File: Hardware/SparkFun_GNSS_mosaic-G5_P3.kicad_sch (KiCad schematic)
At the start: 65 parts, among them J1 USB_C_Receptacle, J10 U.FL, J2 Conn_01x06, J4 Conn_01x10, J5 SMA_Edge, J6 Conn_01x11, J8 JST_Locking_4, U1 DT1042-04SO, U2 RT9080-3.3, U3 mosaic-G5 P3

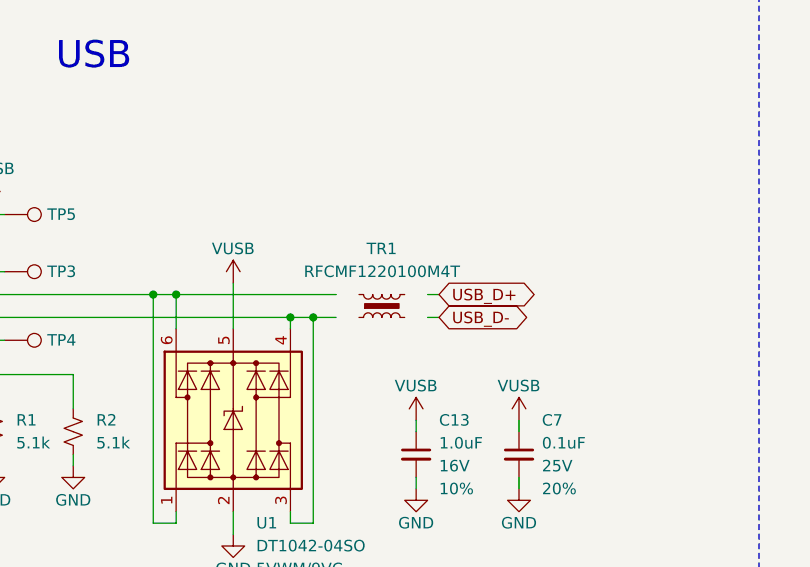
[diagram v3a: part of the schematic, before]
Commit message: Fix RFCMF1220100M4T pin numbering
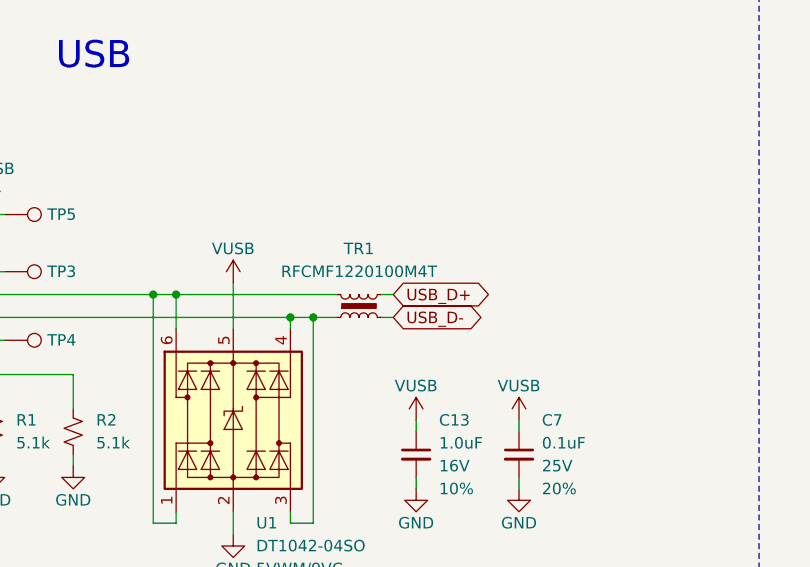
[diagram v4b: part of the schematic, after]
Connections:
- net USB_D+: now also TR1.4
- net USB_D-: now also TR1.2
- net at TR1.1: now also J1.A7 (D-), J1.B7 (D-), TP4.1, U1.3 (I/O2), U1.4 (I/O3)
- net at J1.A6 (D+), J1.B6 (D+), TP3.1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: now also TR1.3
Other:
- moved on the sheet: TR1
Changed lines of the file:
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@@
 	(wire
 		(pts
-			(xy 110.49 52.07) (xy 111.76 52.07)
+			(xy 105.41 52.07) (xy 106.68 52.07)
 		)
 		(stroke
@@
 	(wire
 		(pts
-			(xy 110.49 49.53) (xy 111.76 49.53)
+			(xy 105.41 49.53) (xy 106.68 49.53)
 		)
 		(stroke
@@
 	(global_label "USB_D-"
 		(shape bidirectional)
-		(at 111.76 52.07 0)
+		(at 106.68 52.07 0)
 		(fields_autoplaced yes)
 		(effects
@@
 		)
 		(property "Intersheetrefs" "${INTERSHEET_REFS}"
-			(at 122.6635 52.07 0)
+			(at 117.5835 52.07 0)
 			(effects
 				(font
@@
 	(global_label "USB_D+"
 		(shape bidirectional)
-		(at 111.76 49.53 0)
+		(at 106.68 49.53 0)
 		(fields_autoplaced yes)
 		(effects
@@
 		)
 		(property "Intersheetrefs" "${INTERSHEET_REFS}"
-			(at 122.6635 49.53 0)
+			(at 117.5835 49.53 0)
 			(effects
 				(font
@@
 	(symbol
 		(lib_id "SparkFun-Coil:USB_Transformer")
-		(at 105.41 50.8 0)
+		(at 102.87 50.8 0)
 		(mirror x)
 		(unit 1)
@@
 		(fields_autoplaced yes)
 		(property "Reference" "TR1"
-			(at 105.41 44.45 0)
+			(at 102.87 44.45 0)
 			(effects
 				(font
@@
 		)
 		(property "Value" "RFCMF1220100M4T"
-			(at 105.41 46.99 0)
+			(at 102.87 46.99 0)
 			(effects
 				(font
@@
 		)
 		(property "Footprint" "SparkFun-Coil:Choke_100MHz_USB"
-			(at 104.14 44.45 0)
+			(at 101.6 44.45 0)
 			(effects
 				(font
@@
 		)
 		(property "Datasheet" "http://www.passivecomponent.com/wp-content/uploads/2018/10/RF-Filter.pdf"
-			(at 104.14 41.91 0)
+			(at 101.6 41.91 0)
 			(effects
 				(font
@@
 		)
 		(property "Description" "USB Transformer"
-			(at 105.41 36.83 0)
+			(at 102.87 36.83 0)
 			(effects
 				(font
@@
 		)
 		(property "PROD_ID" "COMP-19495"
-			(at 104.14 39.37 0)
+			(at 101.6 39.37 0)
 			(effects
 				(font
@@
 		(pin "2"
 		)
-		(pin "1"
+		(pin "4"
 		)
-		(pin "2"
+		(pin "3"
 		)
 		(instances

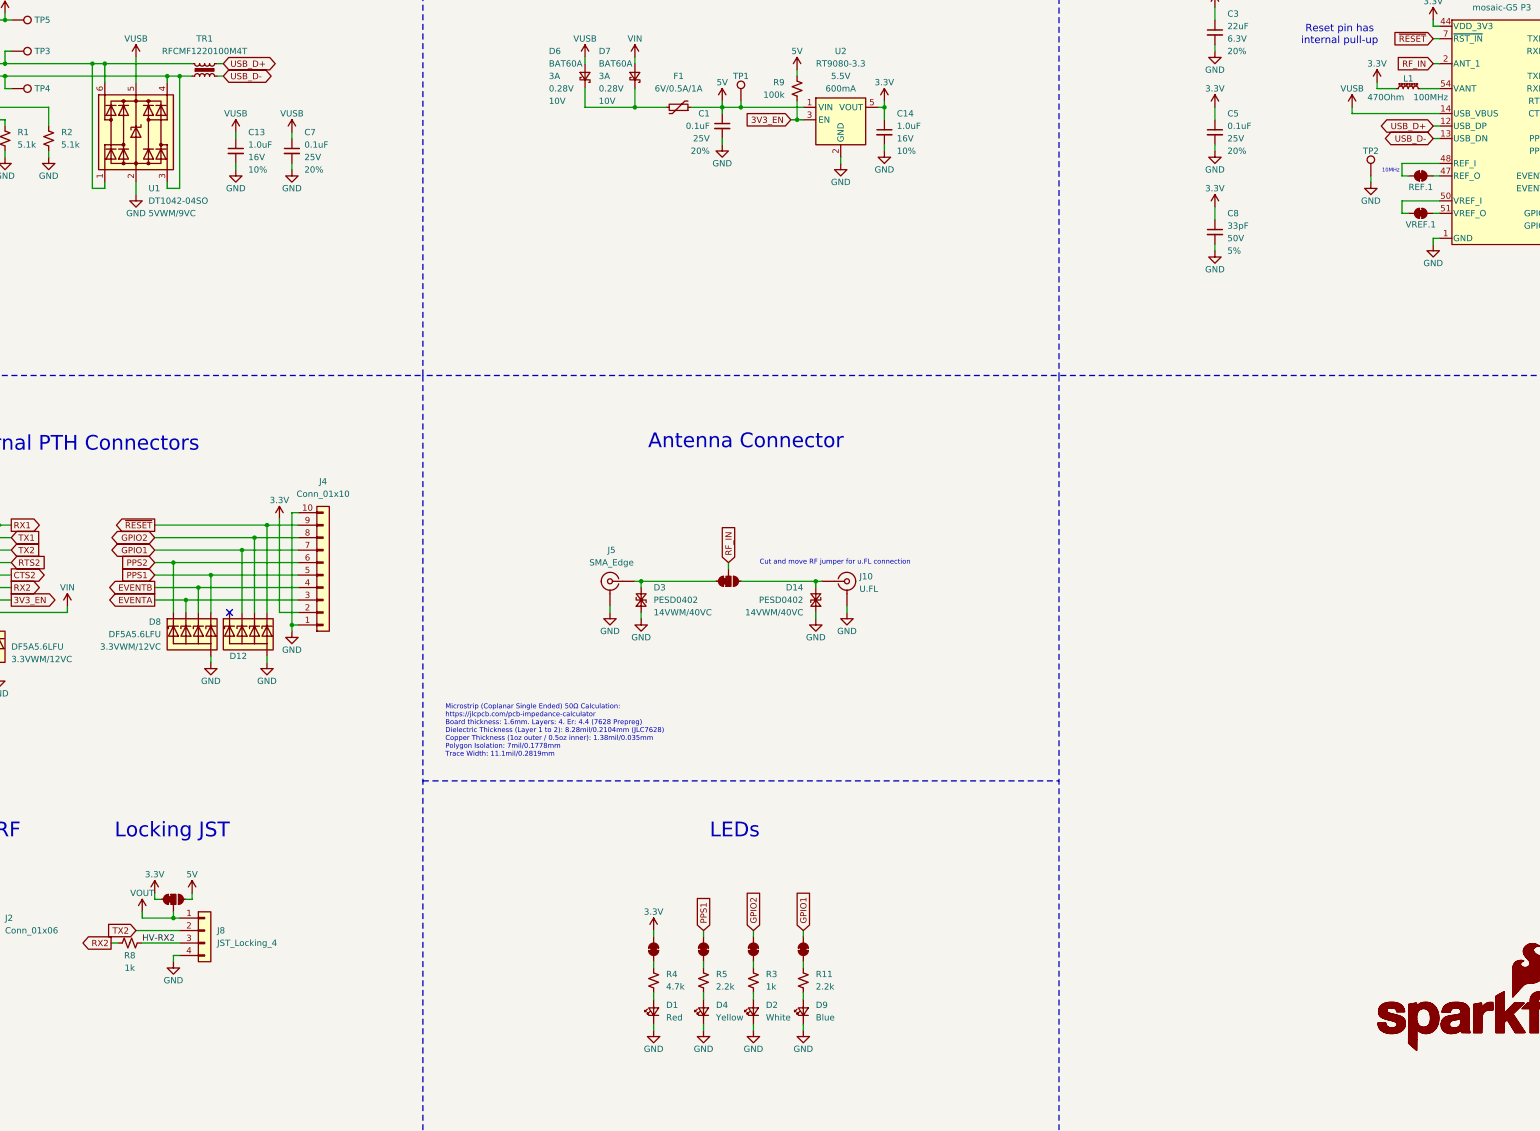
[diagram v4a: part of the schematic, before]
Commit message: Update to latest SparkFun KiCad Libraries
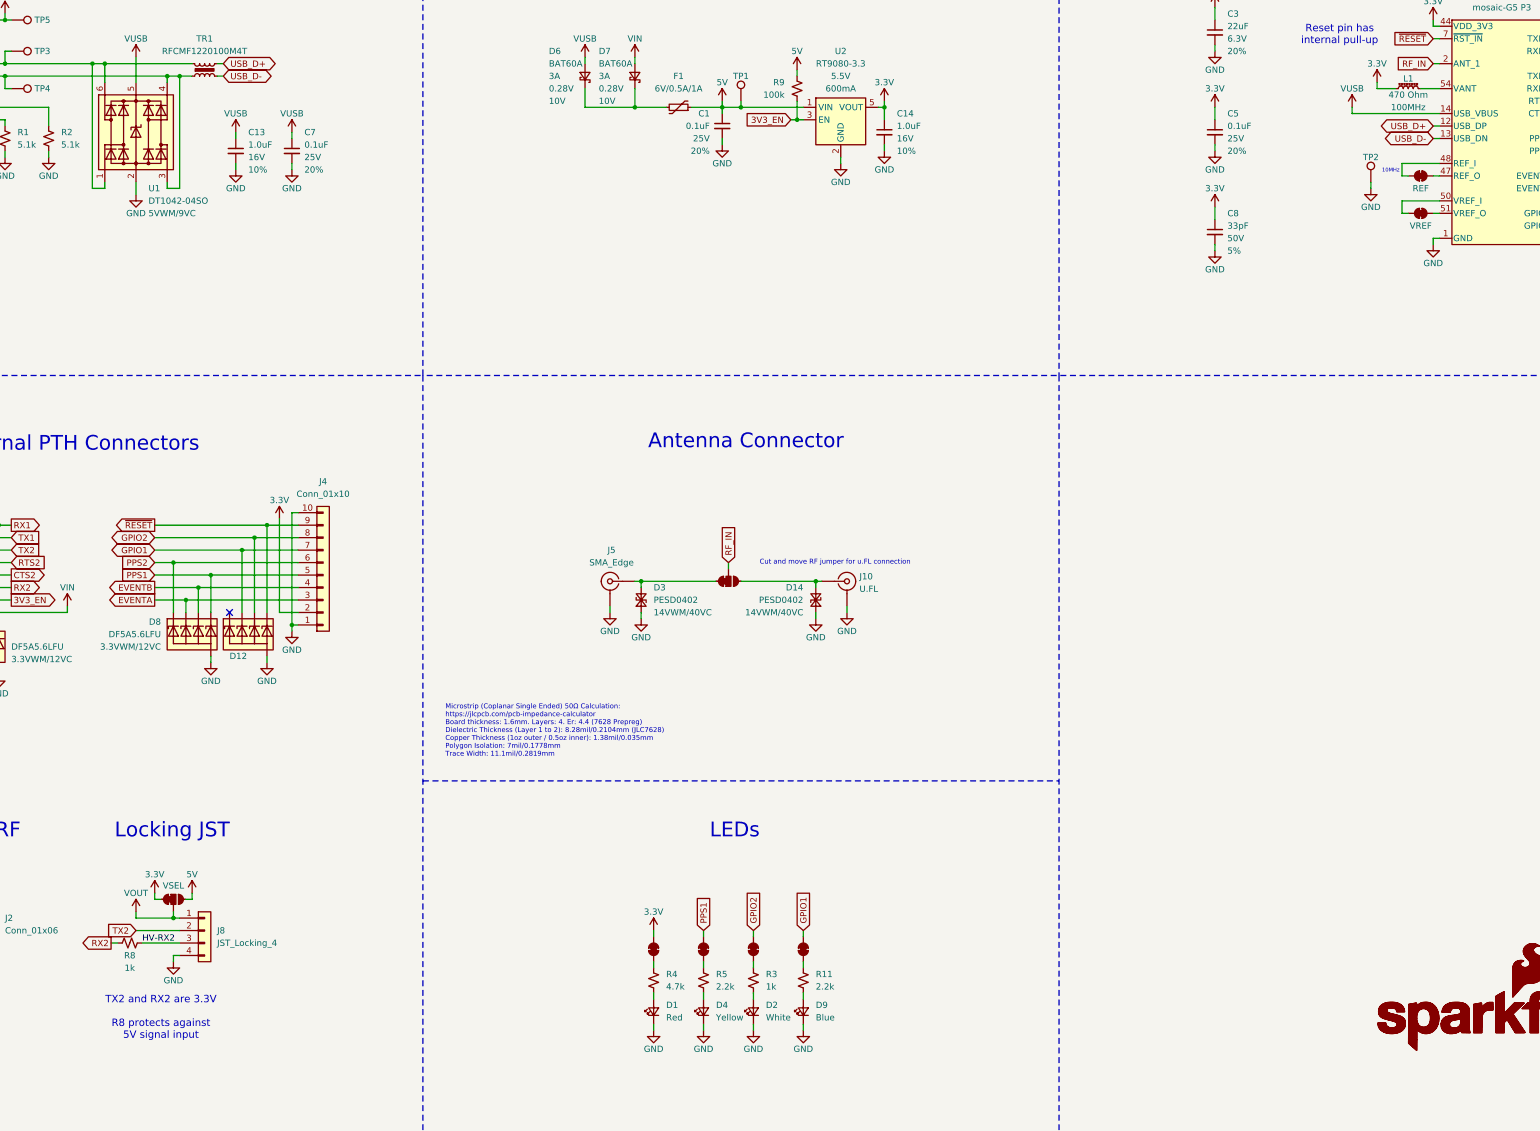
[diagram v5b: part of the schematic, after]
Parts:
- JP4: value ~ -> VSEL
- L1: value 470Ohm -> 470 Ohm; symbol SparkFun-Coil:470Ohm_0603_1.0A -> SparkFun-Coil:Ferrite_470Ohm_0603_1.0A
- REF.1: value ~ -> REF
- U3: footprint SparkFun-GPS:MOSAIC-G5_LGA54 -> SparkFun-GNSS:Septentrio_mosaic-G5_LGA54; symbol SparkFun-GPS:mosaic-G5_P3 -> SparkFun-GNSS:mosaic-G5_P3
- VREF.1: value ~ -> VREF
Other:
- note added: "TX2 and RX2 are 3.3V R8 protects against 5V signal input"
- moved on the sheet: TP2
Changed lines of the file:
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@@
 	(title_block
 		(title "mosaic-G5 P3 Allband GNSS Receiver Breakout")
-		(date "2025-04-23")
+		(date "2025-10-23")
 		(rev "v01")
 		(company "SparkFun Electronics")
 		(comment 1 "Designed by: P.C.")
 	)
+	(text "TX2 and RX2 are 3.3V\n\nR8 protects against\n5V signal input"
+		(exclude_from_sim no)
+		(at 93.98 243.84 0)
+		(effects
+			(font
+				(size 1.5 1.5)
+				(color 132 132 132 1)
+			)
+		)
+	)
 	(text "Microstrip (Coplanar Single Ended) 50Ω Calculation:\nhttps://jlcpcb.com/pcb-impedance-calculator\nBoard thickness: 1.6mm. Layers: 4. Er: 4.4 (7628 Prepreg)\nDielectric Thickness (Layer 1 to 2): 8.28mil/0.2104mm (JLC7628)\nCopper Thickness (1oz outer / 0.5oz inner): 1.38mil/0.035mm\nPolygon Isolation: 7mil/0.1778mm\nTrace Width: 11.1mil/0.2819mm"
 		(exclude_from_sim no)
@@
 			(font
 				(size 1 1)
+				(color 132 132 132 1)
 			)
 			(justify left)
@@
 			(font
 				(size 1 1)
+				(color 132 132 132 1)
 			)
 			(justify left)
@@
 			(font
 				(size 1 1)
+				(color 132 132 132 1)
 			)
 			(justify left)
@@
 			(font
 				(size 1.5 1.5)
+				(color 132 132 132 1)
 			)
 		)
@@
 			(font
 				(size 0.762 0.762)
+				(color 132 132 132 1)
 			)
 		)
@@
 	(wire
 		(pts
-			(xy 90.17 223.52) (xy 90.17 222.25)
+			(xy 88.9 223.52) (xy 88.9 222.25)
 		)
 		(stroke
@@
 	(wire
 		(pts
-			(xy 340.36 72.39) (xy 340.36 73.66)
+			(xy 340.36 73.66) (xy 340.36 74.93)
 		)
 		(stroke
@@
 	(wire
 		(pts
-			(xy 96.52 223.52) (xy 90.17 223.52)
+			(xy 96.52 223.52) (xy 88.9 223.52)
 		)
 		(stroke
@@
 	(symbol
 		(lib_id "SparkFun-Connector:TestPoint_1.25mm")
-		(at 340.36 72.39 0)
+		(at 340.36 73.66 0)
 		(unit 1)
 		(exclude_from_sim no)
@@
 		(fields_autoplaced yes)
 		(property "Reference" "TP2"
-			(at 340.36 67.31 0)
+			(at 340.36 68.58 0)
 			(do_not_autoplace yes)
 			(effects
@@
 		)
 		(property "Value" "1.25mm"
-			(at 340.36 76.2 0)
+			(at 340.36 77.47 0)
 			(effects
 				(font
@@
 		)
 		(property "Footprint" "SparkFun-Connector:TestPoint-1.25mm"
-			(at 340.36 78.74 0)
+			(at 340.36 80.01 0)
 			(effects
 				(font
@@
 		)
 		(property "Datasheet" "~"
-			(at 340.36 80.01 0)
+			(at 340.36 81.28 0)
 			(effects
 				(font
@@
 		)
 		(property "Description" "Test Point"
-			(at 340.36 82.55 0)
+			(at 340.36 83.82 0)
 			(effects
 				(font
@@
 	(symbol
 		(lib_id "SparkFun-PowerSymbol:VOUT")
-		(at 90.17 222.25 0)
+		(at 88.9 222.25 0)
 		(unit 1)
 		(exclude_from_sim no)
@@
 		(fields_autoplaced yes)
 		(property "Reference" "#PWR010"
-			(at 90.17 226.06 0)
+			(at 88.9 226.06 0)
 			(effects
 				(font
@@
 		)
 		(property "Value" "VOUT"
-			(at 90.17 218.44 0)
+			(at 88.9 218.44 0)
 			(do_not_autoplace yes)
 			(effects
@@
 		)
 		(property "Footprint" ""
-			(at 90.17 222.25 0)
+			(at 88.9 222.25 0)
 			(effects
 				(font
@@
 		)
 		(property "Datasheet" ""
-			(at 90.17 222.25 0)
+			(at 88.9 222.25 0)
 			(effects
 				(font
@@
 		)
 		(property "Description" "Power symbol creates a global label with name \"VOUT\""
-			(at 90.17 228.6 0)
+			(at 88.9 228.6 0)
 			(effects
 				(font
@@
 					(size 1.27 1.27)
 				)
+				(hide yes)
 			)
 		)
-		(property "Value" "~"
-			(at 350.52 69.85 0)
+		(property "Value" "REF"
+			(at 350.52 74.93 0)
 			(effects
 				(font
@@
 	)
 	(symbol
-		(lib_id "SparkFun-GPS:mosaic-G5_P3")
+		(lib_id "SparkFun-GNSS:mosaic-G5_P3")
 		(at 367.03 62.23 0)
 		(unit 1)
@@
 			)
 		)
-		(property "Footprint" "SparkFun-GPS:MOSAIC-G5_LGA54"
+		(property "Footprint" "SparkFun-GNSS:Septentrio_mosaic-G5_LGA54"
 			(at 367.03 91.948 0)
 			(effects
@@
 			)
 		)
-		(property "Value" "~"
+		(property "Value" "VSEL"
 			(at 96.52 216.916 0)
 			(effects
@@
 	)
 	(symbol
-		(lib_id "SparkFun-Coil:470Ohm_0603_1.0A")
+		(lib_id "SparkFun-Coil:Ferrite_470Ohm_0603_1.0A")
 		(at 347.98 54.61 0)
 		(unit 1)
@@
 			)
 		)
-		(property "Value" "470Ohm"
-			(at 343.408 56.388 0)
+		(property "Value" "470 Ohm"
+			(at 347.98 55.88 0)
 			(effects
 				(font
@@
 		)
 		(property "Frequency" "100MHz"
-			(at 352.552 56.388 0)
+			(at 347.98 58.42 0)
 			(effects
 				(font
@@
 	(symbol
 		(lib_id "power:GND")
-		(at 340.36 73.66 0)
+		(at 340.36 74.93 0)
 		(unit 1)
 		(exclude_from_sim no)
@@
 		(dnp no)
 		(property "Reference" "#PWR024"
-			(at 340.36 80.01 0)
+			(at 340.36 81.28 0)
 			(effects
 				(font
@@
 		)
 		(property "Value" "GND"
-			(at 340.36 77.47 0)
+			(at 340.36 78.74 0)
 			(effects
 				(font
@@
 		)
 		(property "Footprint" ""
-			(at 340.36 73.66 0)
+			(at 340.36 74.93 0)
 			(effects
 				(font
@@
 		)
 		(property "Datasheet" ""
-			(at 340.36 73.66 0)
+			(at 340.36 74.93 0)
 			(effects
 				(font
@@
 		)
 		(property "Description" "Power symbol creates a global label with name \"GND\" , ground"
-			(at 340.36 73.66 0)
+			(at 340.36 74.93 0)
 			(effects
 				(font
@@
 					(size 1.27 1.27)
 				)
+				(hide yes)
 			)
 		)
-		(property "Value" "~"
-			(at 350.52 77.47 0)
+		(property "Value" "VREF"
+			(at 350.52 82.55 0)
 			(effects
 				(font
